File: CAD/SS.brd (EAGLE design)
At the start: 77 x 99.7 mm, 115 parts, among them Q1 SN74AHC-NOR, Q2 UMD5N, Q5 BFP460, Q6 TCR1HF50, Q7 NCP553, T1 MMBTRA104SS, X1 ANTENNA, X2 RADIO, X3 INP, X4 AMP-O, X5 BPF-O

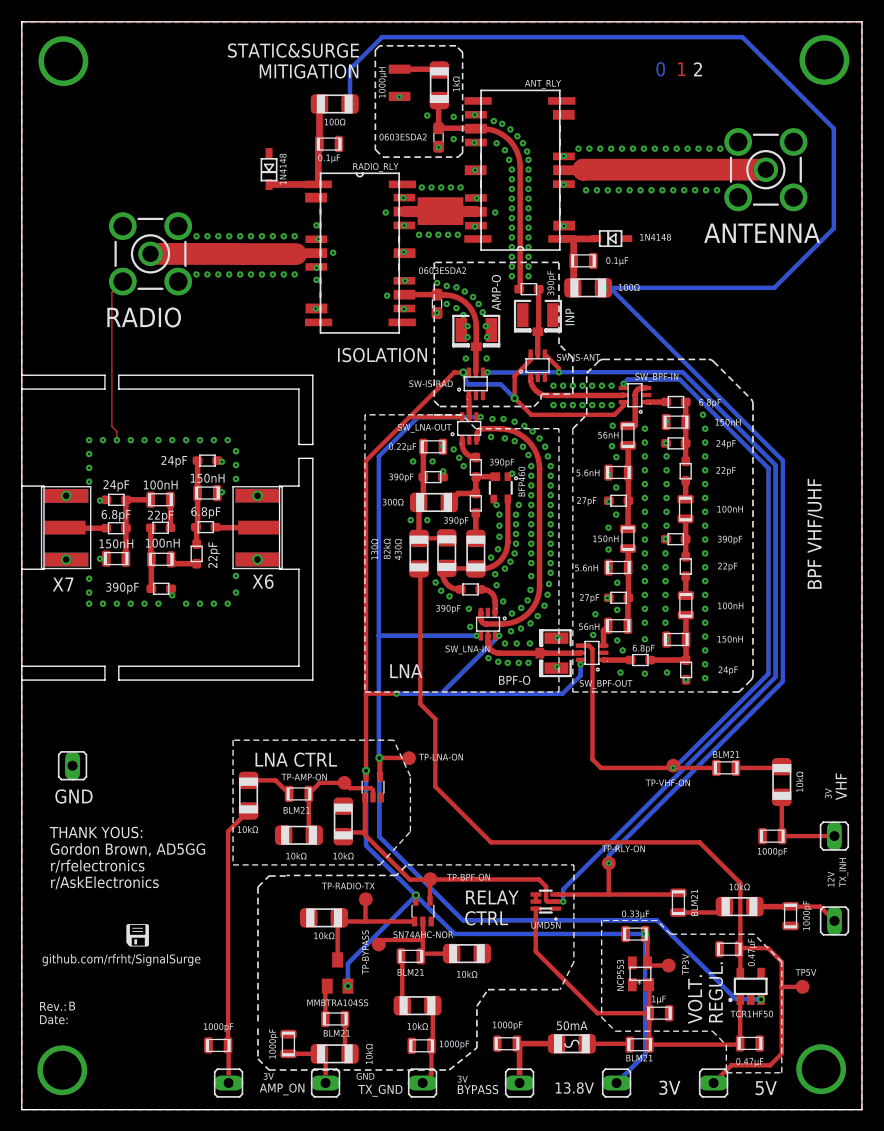
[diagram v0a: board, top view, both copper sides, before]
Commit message: Revision C: Initial launch
For more information, check the changelog.
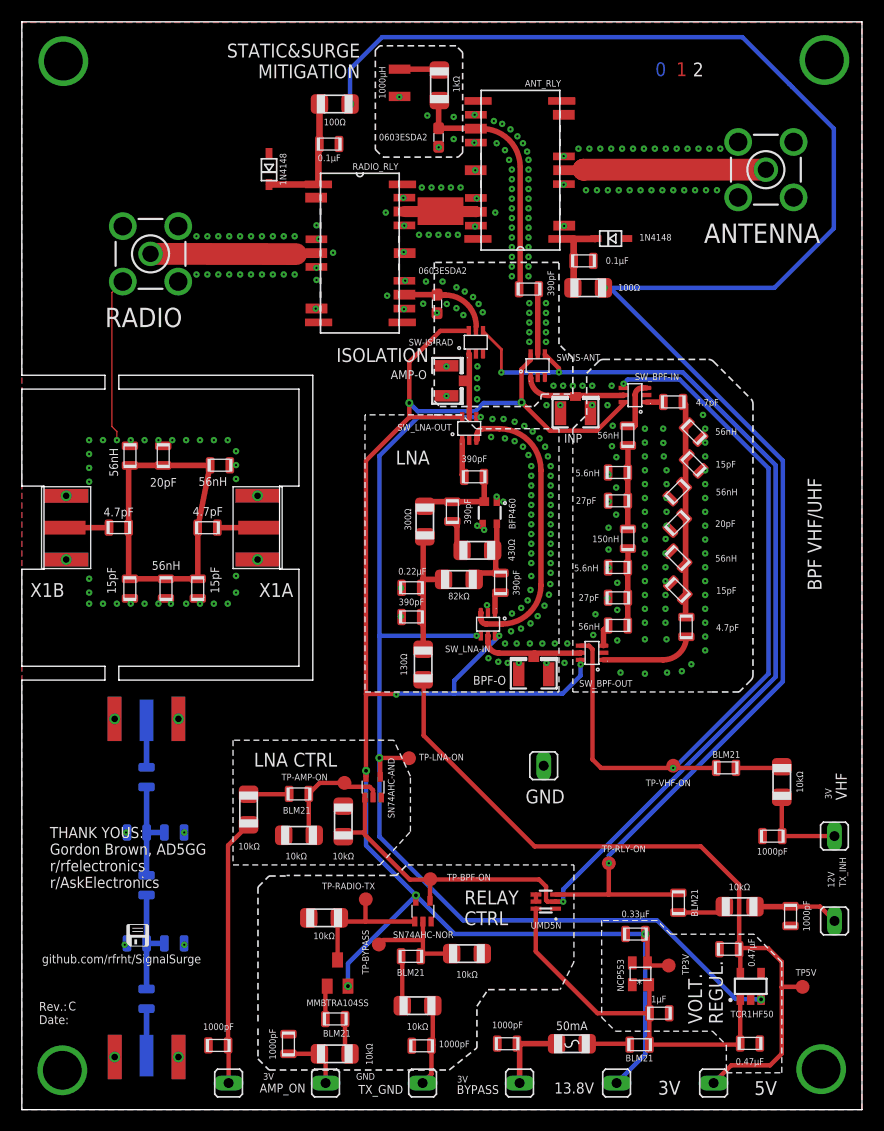
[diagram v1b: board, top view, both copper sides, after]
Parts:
- removed C33: 24pF, aarf:GRM18
- removed C34: 6.8pF, aarf:GRM18
- added L15: 56nH, aarf:0805
- added L16, L17: 5.6nH, aarf:0805
- added X2A, X2B: (no value), aarf:SMA-EDGE
- C1: value 6.8pF -> 4.7pF; device aarf:GRM18 -> aarf:0805
- C10, C12, C25, C6, C7, C8, C9: device aarf:GRM18 -> aarf:0805
- C2, C29: value 24pF -> 15pF; device aarf:GRM18 -> aarf:0805
- C26: value 24pF -> 4.7pF; device aarf:GRM18 -> aarf:0805
- C27: value 6.8pF -> 15pF; device aarf:GRM18 -> aarf:0805
- C28: value 6.8pF -> 20pF; device aarf:GRM18 -> aarf:0805
- C3: value 22pF -> 20pF; device aarf:GRM18 -> aarf:0805
- C30, C5: value 22pF -> 4.7pF; device aarf:GRM18 -> aarf:0805
- C31: value 390pF -> 27pF; device aarf:GRM18 -> aarf:0805
- C32: value 22pF -> 27pF; device aarf:GRM18 -> aarf:0805
- C4: value 390pF -> 15pF; device aarf:GRM18 -> aarf:0805
- L1, L14, L4, L5: value 150nH -> 56nH
- L12, L2, L3: value 100nH -> 56nH
- L13: value 100nH -> 150nH
- Q4: value (none) -> SN74AHC-AND
- moved L4 47.0 mm to (13.2, 47.8), turned to 90 degrees
- moved C26 45.8 mm to (17.0, 53.3), turned to 0 degrees
- moved GND 43.2 mm to (47.8, 31.5)
- moved C27 41.1 mm to (16.1, 47.8), turned to 270 degrees
- moved L13 35.3 mm to (11.4, 20.6), flipped to the bottom, turned to 90 degrees
- moved C31 32.5 mm to (14.0, 15.2), flipped to the bottom
- moved C32 28.0 mm to (10.5, 25.4), flipped to the bottom, turned to 180 degrees
- moved L14 20.2 mm to (11.4, 30.5), flipped to the bottom, turned to 90 degrees
- moved C29 13.7 mm to (9.91, 47.8), turned to 270 degrees
- moved C11 13.1 mm to (35.7, 47.8), turned to 180 degrees
- moved C10 13.0 mm to (35.7, 45.2), turned to 180 degrees
- moved R4 10.2 mm to (36.8, 40.8)
- moved L12 9.93 mm to (9.91, 59.9), turned to 90 degrees
- moved X3 9.63 mm to (50.7, 63.8), turned to 90 degrees
- moved C28 7.63 mm to (13.0, 59.9), turned to 90 degrees
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- renumbered X6 to X1A, X7 to X1B
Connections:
- net N$24 renamed BIAS_IN
- removed net 0: C13.P$1
- removed net N$14: C26.P$1, C27.P$1, L3.P$2, L4.P$1
- removed net N$18: C28.P$1, C29.P$1, C30.P$2, L5.P$2
- removed net N$19: C5.P$2, L3.P$1
- removed net N$20: C30.P$1, L12.P$1
- removed net N$21: C31.P$1, C32.P$1, L12.P$2
- removed net N$23: C33.P$1, C34.P$1, L13.P$2, L14.P$1
- removed net N$25: C32.P$2, L13.P$1
- removed net VHF-IN1: C28.P$2, X1A.P$3
- removed net VHF-OUT1: C34.P$2, X1B.P$3
- new net BPF_VHF: C1.P$1, C2.P$1, C3.P$1, C4.P$1, C5.P$1, L1.P$2, L2.P$2, L3.P$1
- new net N$10: C31.P$2, L13.P$1, L15.P$2, L16.P$1
- new net N$12: L15.P$1, X2A.P$3
- new net N$2: L14.P$2, X2B.P$3
- new net N$9: C32.P$2, L13.P$2, L14.P$1, L17.P$1
- net AMP+BPF_OUT: no longer X4.3
- net BPF_IN: now also X3.3
- net GND: now also C13.P$1, C27.P$2, C28.P$2, C3.P$2, C31.P$1, C32.P$1, L12.P$2, L16.P$2, L17.P$2, L2.P$1, L3.P$2, L4.P$1, X2A.P$1, X2A.P$2, X2A.P$4, X2A.P$5, X2A.P$6, X2A.P$7, X2B.P$1, X2B.P$2, X2B.P$4, X2B.P$5, X2B.P$6, X2B.P$7; no longer C26.P$2, C31.P$2, C33.P$2, L14.P$2, L4.P$2
- net LNA-SW_OUT: now also X4.3
- net N$17: no longer X3.3
- net N$4: now also C26.P$1, C27.P$1, C28.P$1, C29.P$1, C30.P$1, L12.P$1, L4.P$2, L5.P$2; no longer C1.P$1, C2.P$1, C3.P$2, L1.P$2
- net N$5: now also C26.P$2, X1A.P$3; no longer C3.P$1, L2.P$1
- net N$6: now also C30.P$2, X1B.P$3; no longer C4.P$1, C5.P$1, L2.P$2
- net VHF-OUT: now also C5.P$2; no longer C27.P$2
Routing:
- net N$4: track 5.45 -> 34.6 mm
- net BPF_VHF: track 0.00 -> 20.4 mm
- net 5V: track 82.7 -> 70.1 mm
- net N$10: track 0.00 -> 10.3 mm
- net N$9: track 0.00 -> 9.74 mm
- net 3V: track 165.7 -> 175.0 mm
- net N$18: track 7.77 -> 0.00 mm
- net N$23: track 7.65 -> 0.00 mm
- net N$14: track 7.42 -> 0.00 mm
- net VHF-OUT: track 2.48 -> 8.47 mm
- net N$21: track 5.61 -> 0.00 mm
- net LNA-IN: track 13.5 -> 8.60 mm
- net LNA-SW_OUT: track 1.99 -> 6.44 mm
- net N$12: track 0.00 -> 4.31 mm
- net N$2: track 0.00 -> 4.31 mm
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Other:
- outline, holes or cut-outs redrawn
- board text added: "UHF TEST BPF"

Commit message: Board: Refactored the CPWs
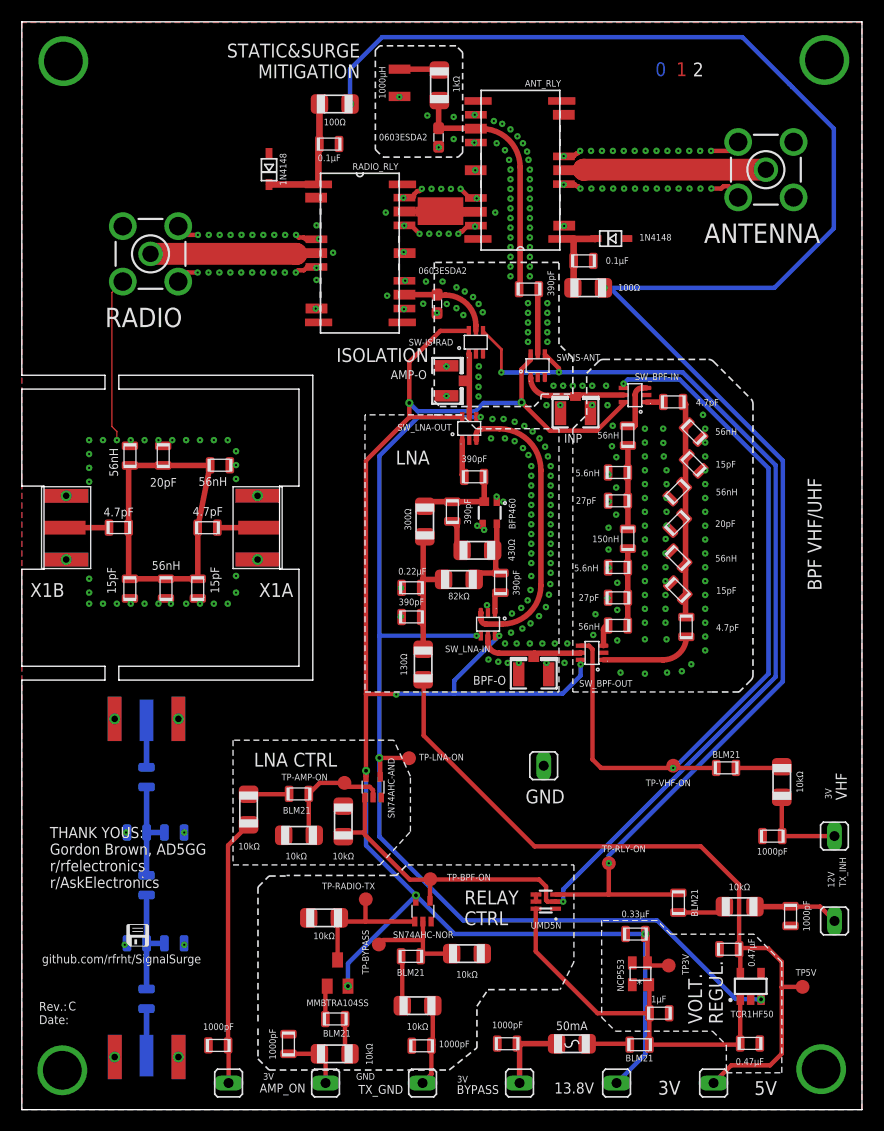
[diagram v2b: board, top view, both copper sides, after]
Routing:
- net GND: track 16.4 -> 41.4 mm, vias 335 -> 334
- net BPF_VHF: track 20.4 -> 22.8 mm
- net TO_BPF: track 22.8 -> 23.3 mm

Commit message: Now: Revision D!
- This is now production grade
- Fixed the pesky UMD5N footprint issue
- Documented thoroughly the BPF and Amplifier performance
- Decoupled the relay logic markdown
- Changed pulldowns on 74XX to 100kR
- More silkscreen, ink for the win
- Resolves: #6, #23, #24
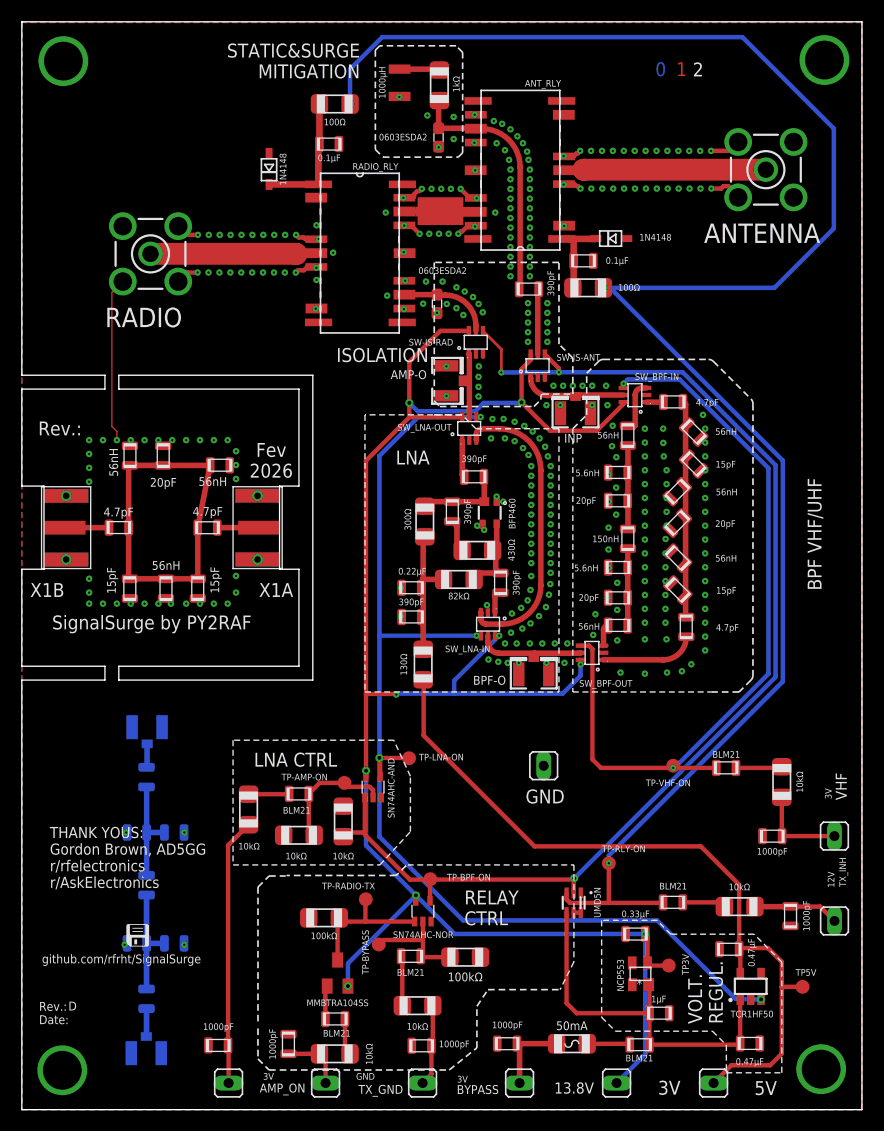
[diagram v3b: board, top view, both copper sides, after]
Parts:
- removed X2A, X2B: (no value), aarf:SMA-EDGE
- added X6, X7: (no value), adafruit:U.FL
- C31, C32, C6, C7: value 27pF -> 20pF
- R13, R14: value 10kΩ -> 100kΩ
- moved Q2 2.56 mm to (50.6, 19.0), turned to 180 degrees
- moved FB2 0.50 mm to (59.7, 19.0), turned to 180 degrees
- moved R14 0.37 mm to (40.6, 14.0), turned to 180 degrees
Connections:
- net 13.8V: now also Q2.4; no longer Q2.6
- net FORCE_BYPASS: now also R14.2; no longer R14.1
- net GND: now also R14.1, X6.1, X6.2, X7.1, X7.2; no longer R14.2, X2A.P$1, X2A.P$2, X2A.P$4, X2A.P$5, X2A.P$6, X2A.P$7, X2B.P$1, X2B.P$2, X2B.P$4, X2B.P$5, X2B.P$6, X2B.P$7
- net N$12: now also L14.P$2, X6.3; no longer L15.P$1, X2A.P$3
- net N$2: now also L15.P$1, X7.3; no longer L14.P$2, X2B.P$3
- net N$7: now also Q2.6; no longer Q2.4
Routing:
- net N$12: track 4.31 -> 2.17 mm
- net N$2: track 4.31 -> 2.56 mm
- net BPF_ON: track 112.5 -> 110.8 mm
- net RELAY-RX_ON: track 165.4 -> 164.5 mm
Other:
- board text added: "Fev 2026"
- board text added: "Rev.:"
- board text added: "SignalSurge by PY2RAF"

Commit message: Revision D: improvements and corrections
* Added a pulldown resistor in the VHF switch line.
* Refactored the CPW between the relays, hoping this tackle the high
  VSWR found in 70 cm band.
* Removed exposed pads that existed in previous version, that might eff up
  and cause capacitive coupling
* Updated RF testing section
* Updated BOM
* Resolves: #26
* Resolves: #28
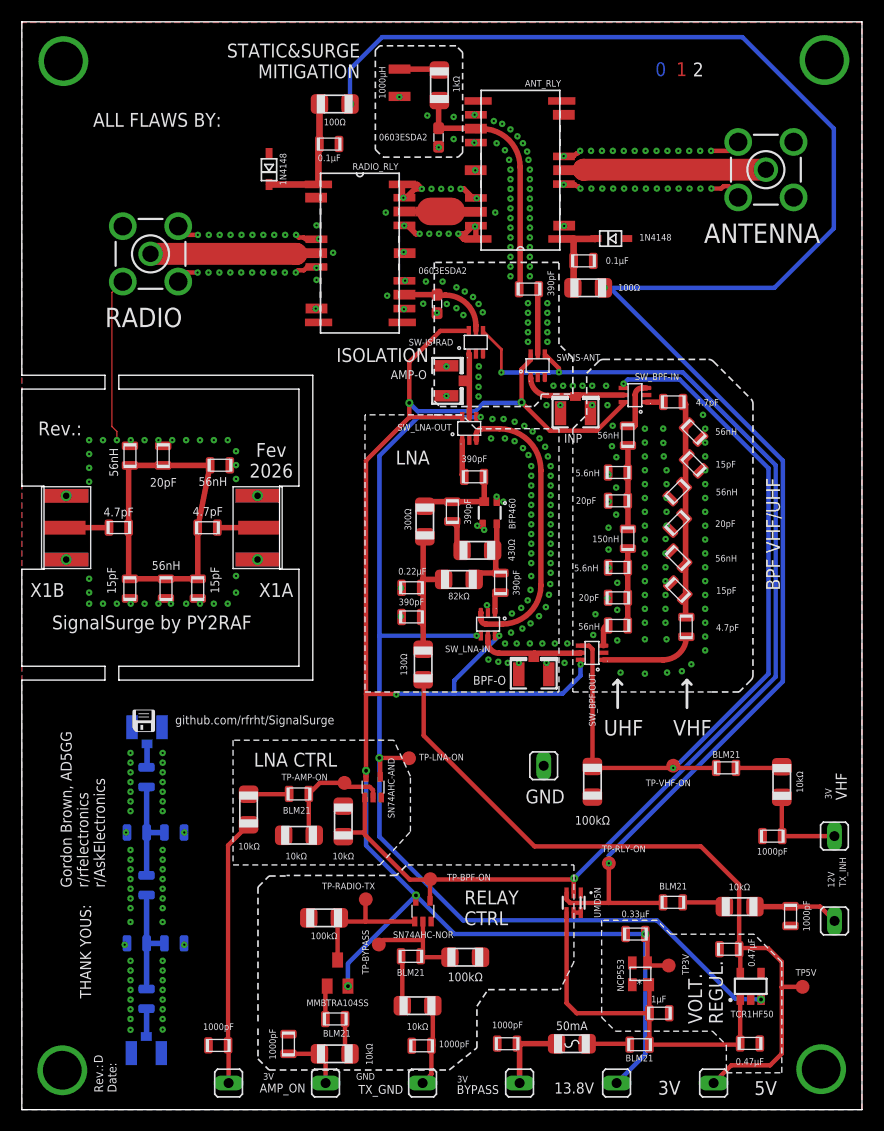
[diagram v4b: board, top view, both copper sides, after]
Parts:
- added R17: 100kΩ, aarf:1206
- renumbered X6 to X2B, X7 to X2A
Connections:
- net GND: now also R17.2
- net SEL_BPF_VHF: now also R17.1
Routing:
- net GND: track 41.4 -> 50.4 mm, vias 334 -> 380
- net N$14: track 0.00 -> 1.90 mm
- net SEL_BPF_VHF: track 71.5 -> 72.2 mm
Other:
- board text added: "ALL FLAWS BY:"
- board text added: "Gordon Brown, AD5GG r/rfelectronics r/AskElectronics"
- board text added: "THANK YOUS:"
- board text added: "UHF"
- board text added: "VHF"
- board text removed: "THANK YOUS: Gordon Brown, AD5GG r/rfelectronics r/AskElectronics"

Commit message: Removed two RF switches
Removed two unneeded RF switches at the front-end: extra cost,
complexity and insertion loss - unnecessarily, as the RF stage
is handsomely isolated - and powered off during high power operations.
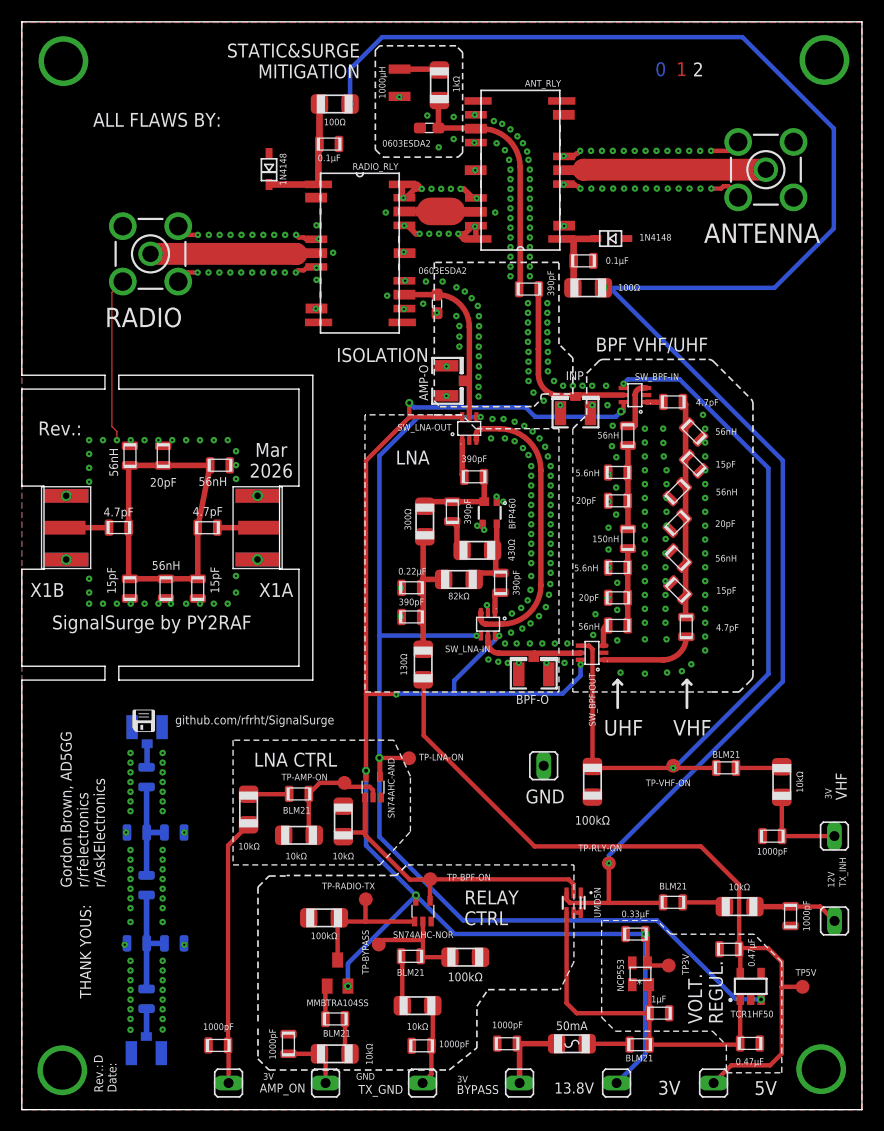
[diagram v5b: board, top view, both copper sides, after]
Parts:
- removed SW-IS-ANT, SW-IS-RAD: PE4259, aarf:SC-70
- moved D1 1.23 mm to (37.3, 90.0), turned to 0 degrees
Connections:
- removed net LNA-SW_OUT: SW-IS-RAD.1, SW_LNA-OUT.5, X4.3
- removed net N$17: C25.P$1, SW-IS-ANT.5
- net 3V: no longer SW-IS-ANT.6, SW-IS-RAD.6
- net AMP+BPF_OUT: now also SW_LNA-OUT.5, X4.3; no longer SW-IS-RAD.5
- net BPF_IN: now also C25.P$1; no longer SW-IS-ANT.1
- net BPF_ON: no longer SW-IS-ANT.4, SW-IS-RAD.4
- net GND: no longer SW-IS-ANT.2, SW-IS-ANT.3, SW-IS-RAD.2, SW-IS-RAD.3
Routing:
- net BPF_ON: track 110.8 -> 29.4 mm, vias 3 -> 0
- net 3V: track 175.0 -> 158.6 mm
- net BPF_IN1: track 0.00 -> 16.1 mm
- net AMP+BPF_OUT1: track 0.00 -> 12.4 mm
- net BPF_IN: track 9.37 -> 1.02 mm
- net LNA-SW_OUT: track 6.42 -> 0.00 mm
- net N$17: track 6.01 -> 0.00 mm
- net AMP+BPF_OUT: track 8.22 -> 3.67 mm
- net UHF-IN1: track 0.00 -> 3.69 mm
- net UHF-IN: track 4.84 -> 1.14 mm
- net GND: vias 380 -> 393
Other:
- board text added: "Mar 2026"
- board text removed: "Fev 2026"
